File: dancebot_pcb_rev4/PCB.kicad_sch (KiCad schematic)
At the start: 52 parts, among them J1 Voltage Regulator, J10 NeoPixel Right Eye, J11 Rocker Switch, J2 IO14 servo 1, J3 IO13 servo 2, J4 IO12 servo 3, J5 IO15 servo 4, J6 IO18 servo 5 (hat), J7 UJ2-MIBH2-4-SMT-TR, J8 Pins, J9 NeoPixel Left Eye, Q1 IRLML6402TRPBF, Q2 S8050, Q3 S8050, SW1 RESET, SW2 BOOT, U1 IRLML2502TRPBF, U2 AMS1117-3.3, U3 ESP32-WROOM-32E__4MB_, U4 CP2102N-A02-GQFN28R

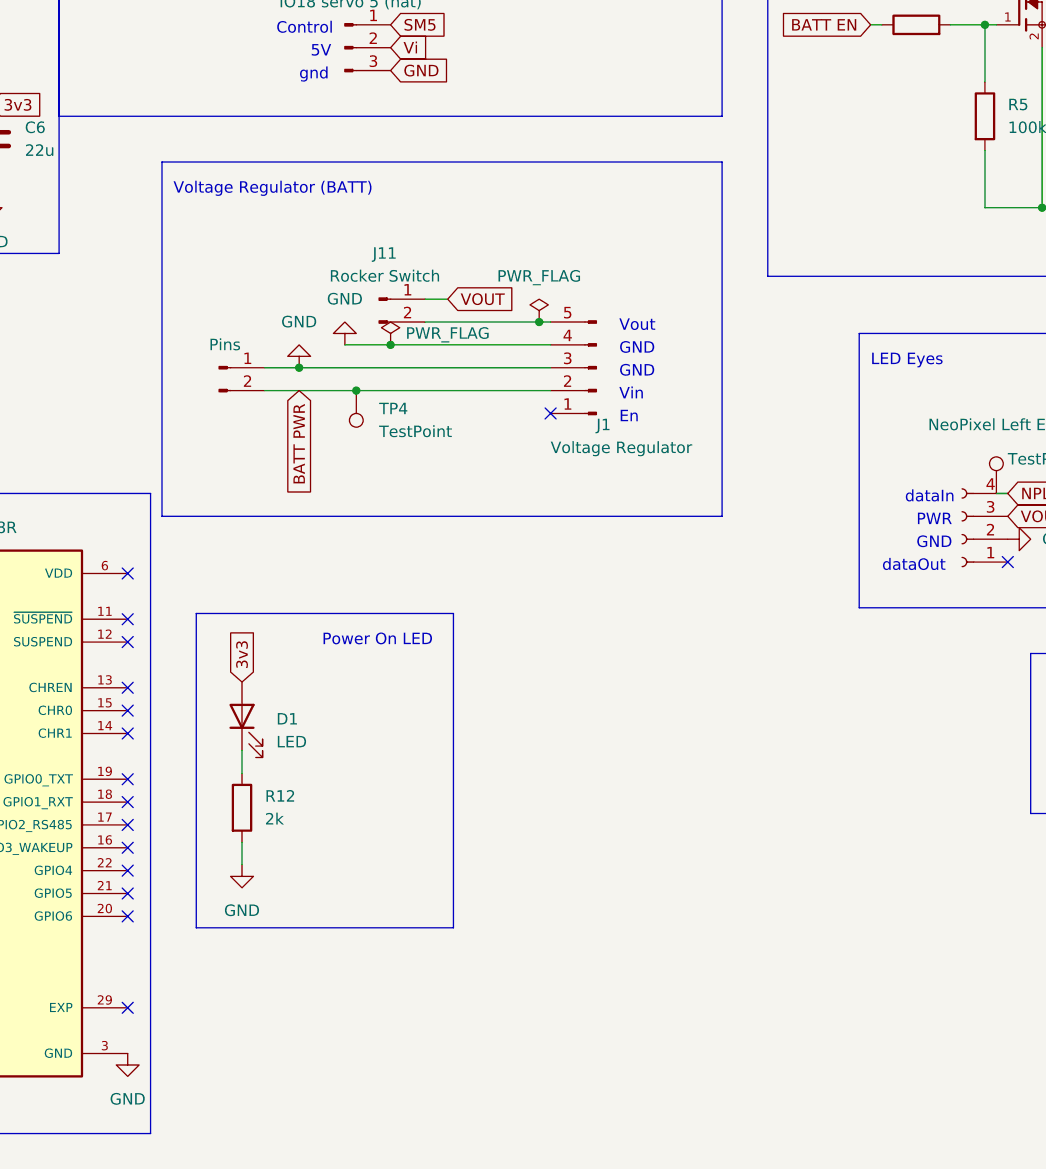
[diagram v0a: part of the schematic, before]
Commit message: added rocker switch
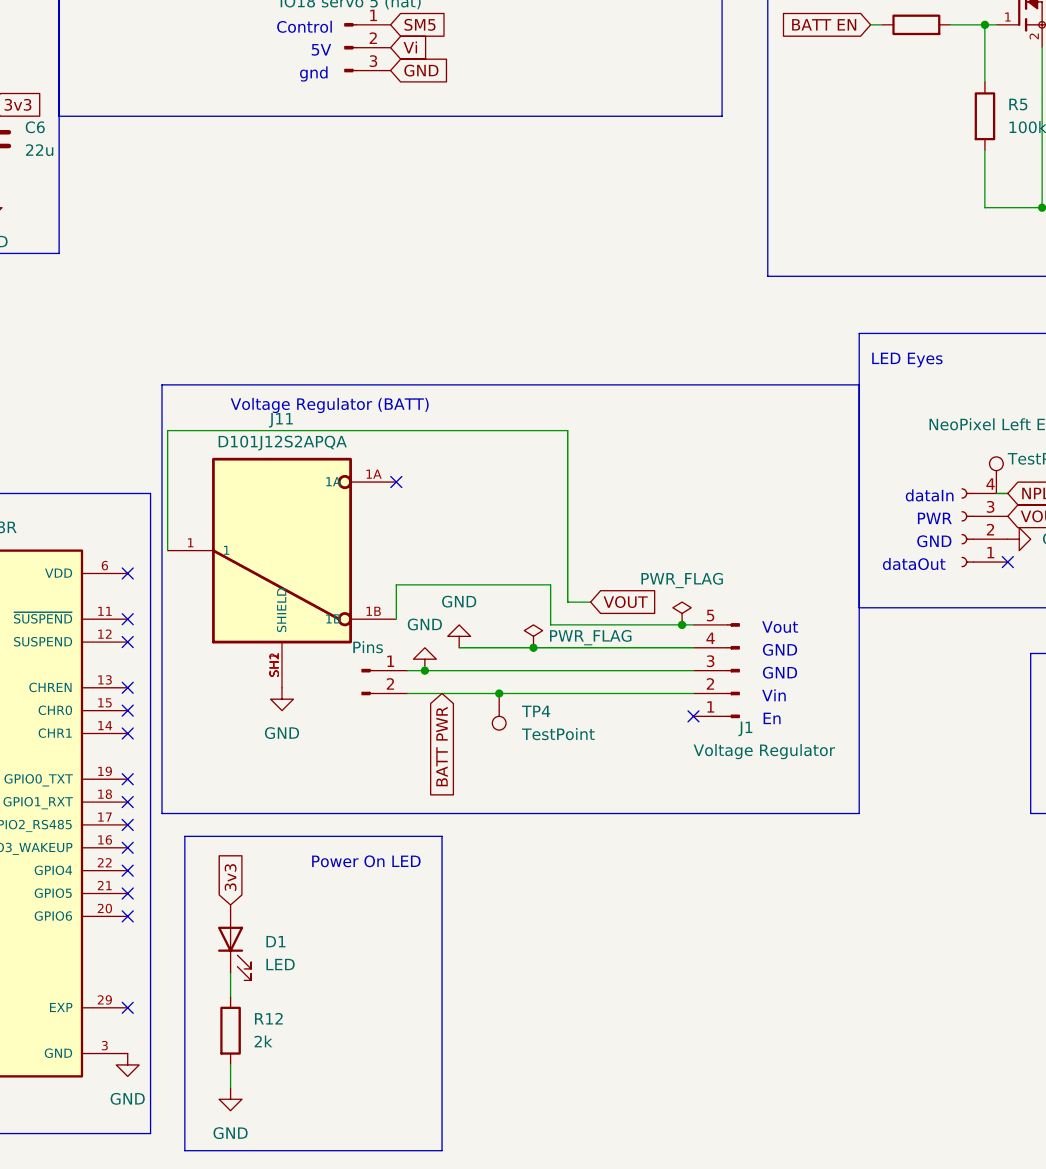
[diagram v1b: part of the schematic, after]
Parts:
- removed J11: Rocker Switch, Connector_PinHeader_2.54mm:PinHeader_1x02_P2.54mm_Vertical, symbol Connector:Conn_01x02_Pin
- added J11: D101J12S2APQA, D101J12S2APQA:D101J12S2APQA, symbol Rocker_Switch:D101J12S2APQA
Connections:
- net GND: now also J11.SH1 (SHIELD), J11.SH2 (SHIELD)
- net VOUT: now also J11.1
- net at J1.5 (Pin_5): now also J11.1B
- no-connect marks 36 -> 37
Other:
- moved on the sheet: D1, J1, R12, TP4

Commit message: fixed stuff
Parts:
- C9: footprint (none) -> Capacitor_SMD:C_0805_2012Metric
- J11: footprint D101J12S2APQA:D101J12S2APQA -> dancebot_parts:D101J12S2APQA
- Q2, Q3: footprint Package_TO_SOT_THT:TO-92_Inline -> Package_TO_SOT_SMD:SOT-23
- U2: footprint AMS1117-3.3:SOT229P700X180-4N -> dancebot_parts:SOT229P700X180-4N
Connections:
- net Vi is gone; now on net VBUS: J2.2 (Pin_2), J3.2 (Pin_2), J4.2 (Pin_2), J5.2 (Pin_2), J6.2 (Pin_2)
- net VBUS: now also J10.3 (Pin_3), J9.3 (Pin_3)
- net VOUT: no longer J10.3 (Pin_3), J9.3 (Pin_3)
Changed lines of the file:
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@@
     )
   )
-  (global_label "VOUT" (shape input) (at 233.68 124.46 0) (fields_autoplaced)
-    (effects (font (size 1.27 1.27)) (justify left))
-    (property "Intersheetrefs" "${INTERSHEET_REFS}" (at 241.3824 124.46 0)
+  (global_label "VBUS" (shape input) (at 233.68 124.46 0) (fields_autoplaced)
+    (effects (font (size 1.27 1.27)) (justify left))
+    (property "Intersheetrefs" "${INTERSHEET_REFS}" (at 241.5638 124.46 0)
       (effects (font (size 1.27 1.27)) (justify left) hide)
     )
@@
     )
   )
-  (global_label "VOUT" (shape input) (at 265.43 124.46 0) (fields_autoplaced)
-    (effects (font (size 1.27 1.27)) (justify left))
-    (property "Intersheetrefs" "${INTERSHEET_REFS}" (at 273.1324 124.46 0)
-      (effects (font (size 1.27 1.27)) (justify left) hide)
-    )
-  )
-  (global_label "Vi" (shape input) (at 176.53 54.61 0) (fields_autoplaced)
-    (effects (font (size 1.27 1.27)) (justify left))
-    (property "Intersheetrefs" "${INTERSHEET_REFS}" (at 181.2086 54.61 0)
-      (effects (font (size 1.27 1.27)) (justify left) hide)
-    )
-  )
-  (global_label "Vi" (shape input) (at 151.13 54.61 0) (fields_autoplaced)
-    (effects (font (size 1.27 1.27)) (justify left))
-    (property "Intersheetrefs" "${INTERSHEET_REFS}" (at 155.8086 54.61 0)
+  (global_label "VBUS" (shape input) (at 265.43 124.46 0) (fields_autoplaced)
+    (effects (font (size 1.27 1.27)) (justify left))
+    (property "Intersheetrefs" "${INTERSHEET_REFS}" (at 273.3138 124.46 0)
+      (effects (font (size 1.27 1.27)) (justify left) hide)
+    )
+  )
+  (global_label "VBUS" (shape input) (at 176.53 54.61 0) (fields_autoplaced)
+    (effects (font (size 1.27 1.27)) (justify left))
+    (property "Intersheetrefs" "${INTERSHEET_REFS}" (at 184.4138 54.61 0)
+      (effects (font (size 1.27 1.27)) (justify left) hide)
+    )
+  )
+  (global_label "VBUS" (shape input) (at 151.13 54.61 0) (fields_autoplaced)
+    (effects (font (size 1.27 1.27)) (justify left))
+    (property "Intersheetrefs" "${INTERSHEET_REFS}" (at 159.0138 54.61 0)
       (effects (font (size 1.27 1.27)) (justify left) hide)
     )
@@
     )
   )
-  (global_label "Vi" (shape input) (at 152.4 35.56 0) (fields_autoplaced)
-    (effects (font (size 1.27 1.27)) (justify left))
-    (property "Intersheetrefs" "${INTERSHEET_REFS}" (at 157.0786 35.56 0)
-      (effects (font (size 1.27 1.27)) (justify left) hide)
-    )
-  )
-  (global_label "Vi" (shape input) (at 165.1 72.39 0) (fields_autoplaced)
-    (effects (font (size 1.27 1.27)) (justify left))
-    (property "Intersheetrefs" "${INTERSHEET_REFS}" (at 169.7786 72.39 0)
+  (global_label "VBUS" (shape input) (at 152.4 35.56 0) (fields_autoplaced)
+    (effects (font (size 1.27 1.27)) (justify left))
+    (property "Intersheetrefs" "${INTERSHEET_REFS}" (at 160.2838 35.56 0)
+      (effects (font (size 1.27 1.27)) (justify left) hide)
+    )
+  )
+  (global_label "VBUS" (shape input) (at 165.1 72.39 0) (fields_autoplaced)
+    (effects (font (size 1.27 1.27)) (justify left))
+    (property "Intersheetrefs" "${INTERSHEET_REFS}" (at 172.9838 72.39 0)
       (effects (font (size 1.27 1.27)) (justify left) hide)
     )
@@
     )
   )
-  (global_label "Vi" (shape input) (at 176.53 35.56 0) (fields_autoplaced)
-    (effects (font (size 1.27 1.27)) (justify left))
-    (property "Intersheetrefs" "${INTERSHEET_REFS}" (at 181.2086 35.56 0)
+  (global_label "VBUS" (shape input) (at 176.53 35.56 0) (fields_autoplaced)
+    (effects (font (size 1.27 1.27)) (justify left))
+    (property "Intersheetrefs" "${INTERSHEET_REFS}" (at 184.4138 35.56 0)
       (effects (font (size 1.27 1.27)) (justify left) hide)
     )
@@
       (effects (font (size 1.27 1.27)))
     )
-    (property "Footprint" "AMS1117-3.3:SOT229P700X180-4N" (at 101.6 81.28 0)
+    (property "Footprint" "dancebot_parts:SOT229P700X180-4N" (at 101.6 81.28 0)
       (effects (font (size 1.27 1.27)) (justify bottom) hide)
     )
@@
       (effects (font (size 1.27 1.27)) (justify left))
     )
-    (property "Footprint" "Package_TO_SOT_THT:TO-92_Inline" (at 48.26 103.505 0)
+    (property "Footprint" "Package_TO_SOT_SMD:SOT-23" (at 48.26 103.505 0)
       (effects (font (size 1.27 1.27) italic) (justify left) hide)
     )
@@
       (effects (font (size 1.27 1.27)) (justify left))
     )
-    (property "Footprint" "" (at 23.1902 38.1 0)
+    (property "Footprint" "Capacitor_SMD:C_0805_2012Metric" (at 23.1902 38.1 0)
       (effects (font (size 1.27 1.27)) hide)
     )
@@
       (effects (font (size 1.27 1.27)))
     )
-    (property "Footprint" "D101J12S2APQA:D101J12S2APQA" (at 153.035 128.27 0)
+    (property "Footprint" "dancebot_parts:D101J12S2APQA" (at 153.035 128.27 0)
       (effects (font (size 1.27 1.27)) (justify bottom) hide)
     )
@@
       (effects (font (size 1.27 1.27)) (justify left))
     )
-    (property "Footprint" "Package_TO_SOT_THT:TO-92_Inline" (at 48.26 116.205 0)
+    (property "Footprint" "Package_TO_SOT_SMD:SOT-23" (at 48.26 116.205 0)
       (effects (font (size 1.27 1.27) italic) (justify left) hide)
     )

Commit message: Current PCB Progress
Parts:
- removed J11: D101J12S2APQA, dancebot_parts:D101J12S2APQA, symbol Rocker_Switch:D101J12S2APQA
- added J11: Rocker Switch, Connector_PinHeader_2.54mm:PinHeader_1x02_P2.54mm_Vertical, symbol Connector:Conn_01x02_Pin
- J7: footprint dancebot_parts:CUI_UJ2-MIBH2-4-SMT-TR -> UJ2-MIBH-4-SMT-TR:CUIDEVICES_UJ2-MIBH-4-SMT-TR
- Q1: footprint dancebot_parts:SOT95P237X112-3N -> IRLML6402TRPBF:SOT95P237X112-3N
- Q2, Q3: footprint Package_TO_SOT_SMD:SOT-23 -> Package_TO_SOT_THT:TO-92_Inline
- U1: footprint dancebot_parts:SOT23 -> IRLML2502TRPBF:SOT23
- U2: footprint dancebot_parts:SOT229P700X180-4N -> AMS1117-3.3:SOT229P700X180-4N
- U3: footprint dancebot_parts:XCVR_ESP32-WROOM-32E__4MB_ -> ESP32-WROOM-32E__4MB_:XCVR_ESP32-WROOM-32E__4MB_
- U4: footprint dancebot_parts:IC_CP2102N-A02-GQFN28R -> CP2102N-A02-GQFN28R:IC_CP2102N-A02-GQFN28R
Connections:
- net VBUS: no longer J10.3 (Pin_3), J9.3 (Pin_3)
- net VOUT: now also J10.3 (Pin_3), J9.3 (Pin_3), J11.1 (Pin_1)
- net at J1.5 (Pin_5): now also J11.2 (Pin_2)
- no-connect marks 37 -> 36
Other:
- moved on the sheet: D1, J1, R12, TP4
